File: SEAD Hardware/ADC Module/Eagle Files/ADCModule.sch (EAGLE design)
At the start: 51 parts, among them U1 ADS8568_PM_64, U2 LP2950-3.3ACZ

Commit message: Started SPI/USB Bridge
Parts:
- added C18: 10nF, SensorCape:CAP0805
- added C19, C20: 47pF, SensorCape:CAP0805
- added C21, C23, C24: 100nF, SensorCape:CAP0805
- added C22: 4.7uF, SensorCape:CAP_POLPTH2
- added L1: Ferrite Bead 0805, ASL:INDUCTOR0805
- added R4, R5: 27 1%, SensorCape:RESISTOR0805-RES
- added U$2: FT121Q, SensorCape:FT121Q
- added U3: SI8663BC-B-IS1, SensorCape:SI8663BC-B-IS1
- added X1: MINI-USB-SCHIELD-32005-201, con-cypressindustries:MINI-USB-SCHIELD-32005-201
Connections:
- new net GND_USB: C18.2, C19.1, C20.2, C21.1, C22.-, C23.1, U$2.GND, U$2.GND1, U3.GND1, X1G$1.5, X1S.S1, X1S.S2, X1S.S3, X1S.S4
- new net N$10: R4.2, U$2.DM
- new net N$11: U$2.SS_N
- new net N$12: R5.2, U$2.DP
- new net N$13: U$2.MISO, U3.A3
- new net N$17: U$2.MOSI, U3.A6
- new net N$18: U$2.SCLK, U3.A4
- new net N$19: U3.A5
- new net N$6: C18.1, L1.1, X1G$1.1
- new net N$8: C19.2, R4.1, X1G$1.2
- new net N$9: C20.1, R5.1, X1G$1.3
- new net SCLK: U3.B4
- new net VCC3V3_USB: C21.2, C24.1, C24.2, U$2.RESET_N, U$2.VBUS_S, U$2.VCCIO, U$2.VOUT3V3, U3.VDD1
- new net VCC_USB: C22.+, C23.2, L1.2, U$2.VCC
- net MISO: now also U3.B3
- net MOSI: now also U3.B6

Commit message: Finished DAQ Hardware v1.4 and Filtering Simulations
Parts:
- removed C72, C73, C74: 10nF, SensorCape:CAP0805
- removed JP4: (no value), ASL:M06SIP
- removed JP5: M03PTH, ASL:M03PTH
- removed L1: Ferrite Bead 0805, ASL:INDUCTOR0805
- removed R4, R5: 27 1%, SensorCape:RESISTOR0805-RES
- removed U3: SI8663BC-B-IS1, SensorCape:SI8663BC-B-IS1
- removed X1: MINI-USB-SCHIELD-32005-201, con-cypressindustries:MINI-USB-SCHIELD-32005-201
- added C25, C26, C27, C29, C32: 10uF, ASL:CAP0805
- added C30: 1uF, SensorCape:CAP0805
- added C31: 10nF, SensorCape:CAP0805
- added C34: 10uF, SensorCape:CAP1206
- added JP2: M03-SCREW-5MM, ASL:M03-SCREW-5MM
- added R23: 1.5M, ASL:RESISTOR0805-RES
- added R24: 162k, ASL:RESISTOR0805-RES
- added U6: TPS7A3301_RGW_20, SensorCape:TPS7A3301_RGW_20
- C18: value 10nF -> 1uF
- C19: value 47pF -> 10uF; device SensorCape:CAP0805 -> SensorCape:CAP1206
- C20: value 47pF -> 10uF; device SensorCape:CAP0805 -> ASL:CAP0805
- C21, C23, C24: value 100nF -> 10uF; device SensorCape:CAP0805 -> ASL:CAP0805
- C22: value 4.7uF -> 10uF; device SensorCape:CAP_POLPTH2 -> ASL:CAP0805
- U$2: value FT121Q -> TPS7A4700_RGW_20; device SensorCape:FT121Q -> SensorCape:TPS7A4700_RGW_20
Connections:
- removed net AA1_R_OUT: C73.2, JP4.1, U1.CH_A0
- removed net AA2_R_OUT: C74.2, JP4.3, U1.CH_A1
- removed net AA3_R_OUT: C72.2, JP4.5, U1.CH_B0
- removed net GND_USB: C18.2, C19.1, C20.2, C21.1, C22.-, C23.1, U$2.GND, U$2.GND1, U3.GND1, X1G$1.5, X1S.S1, X1S.S2, X1S.S3, X1S.S4
- removed net N$1: JP1.3, JP4.2
- removed net N$10: R4.2, U$2.DM
- removed net N$11: U$2.SS_N
- removed net N$12: R5.2, U$2.DP
- removed net N$13: U$2.MISO, U3.A3
- removed net N$17: U$2.MOSI, U3.A6
- removed net N$18: U$2.SCLK, U3.A4
- removed net N$19: U3.A5
- removed net N$2: JP1.2, JP4.4
- removed net N$3: JP1.1, JP4.6
- removed net N$9: C20.1, R5.1, X1G$1.3
- removed net SCLK: U3.B4
- removed net VCC3V3_USB: C21.2, C24.1, C24.2, U$2.RESET_N, U$2.VBUS_S, U$2.VCCIO, U$2.VOUT3V3, U3.VDD1
- removed net VCC_USB: C22.+, C23.2, L1.2, U$2.VCC
- new net A0: JP1.3, U1.CH_A0
- new net A1: JP1.2, U1.CH_A1
- new net B0: JP1.1, U1.CH_B0
- new net B1: JP2.3, U1.CH_B1
- new net C0: JP2.2, U1.CH_C0
- new net C1: JP2.1, U1.CH_C1
- new net D0: U1.CH_D0
- new net D1: U1.CH_D1
- new net HVDD_15D: C19.1, U$2.EN, U$2.IN, U$2.IN_2
- new net HVSS_15D: C34.2, U6.EN, U6.IN, U6.IN_2
- new net N$33: C30.1, U6.NR/SS
- net GND: now also C18.2, C19.2, C20.2, C21.2, C22.2, C23.2, C24.2, C25.2, C26.2, C27.2, C29.2, C30.2, C32.2, C34.1, R24.1, U$2.0P2V, U$2.0P8V, U$2.3P2V, U$2.6P4V2, U$2.EPAD, U$2.GND, U6.EPAD, U6.GND; no longer C72.1, C73.1, C74.1, JP5.3, U1.CH_B1, U1.CH_C0, U1.CH_C1, U1.CH_D0, U1.CH_D1
- net HVDD_12A: now also C20.1, C21.1, C22.1, C23.1, C24.1, U$2.OUT, U$2.OUT_1, U$2.SENSE/FB; no longer JP5.2
- net HVSS_12A: now also C25.1, C26.1, C27.1, C29.1, C31.1, C32.1, R23.2, U6.OUT, U6.OUT_2; no longer JP5.1
- net MISO: no longer U3.B3
- net MOSI: no longer U3.B6
- net N$6: now also U$2.NR; no longer L1.1, X1G$1.1
- net N$8: now also C31.2, R23.1, R24.2, U6.FB; no longer C19.2, R4.1, X1G$1.2
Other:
- moved on the sheet: C18, C19, C20, C21, C23, C24

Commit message: More compute unit work.
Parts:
- removed C1, C2, C3, C4, C46, C47, C48, C5, C53, C54, C56, C6, C7: 10uF, SensorCape:CAP0805
- removed C18, C28, C30, C58: 1uF, SensorCape:CAP0805
- removed C19, C34: 10uF, SensorCape:CAP1206
- removed C20, C21, C22, C23, C24, C25, C26, C27, C29, C32: 10uF, ASL:CAP0805
- removed C31: 10nF, SensorCape:CAP0805
- removed C33: 10uF, SensorCape:CAP_POLPTH2
- removed C55, C57, C59, C60, C61, C62, C64, C71: .1uF, SensorCape:CAP0805
- removed C63: .47uF, SensorCape:CAP0805
- removed JP1, JP2: M03-SCREW-5MM, ASL:M03-SCREW-5MM
- removed R23: 1.5M, ASL:RESISTOR0805-RES
- removed R24: 162k, ASL:RESISTOR0805-RES
- removed SL1: (no value), ASL:M04LOCK
- removed U$2, U$3: TPS7A4700_RGW_20, SensorCape:TPS7A4700_RGW_20
- removed U1: ADS8568_PM_64, SensorCape:ADS8568_PM_64
- removed U2: LP2950-3.3ACZ, ASL:LP2950-3.3ACZ
- removed U6: TPS7A3301_RGW_20, SensorCape:TPS7A3301_RGW_20
- added X1: 52885-0374, SensorCape:52885-0374
- C8: device SensorCape:CAP1206 -> SensorCape:CAP0805
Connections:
- removed net A0: JP1.3, U1.CH_A0
- removed net A1: JP1.2, U1.CH_A1
- removed net B0: JP1.1, U1.CH_B0
- removed net B1: JP2.3, U1.CH_B1
- removed net BUSY: U$1.AETXD0/*SS1A/U1BRX/*U1ACTS/CN20/RD14, U1.BUSY/INT
- removed net C0: JP2.2, U1.CH_C0
- removed net C1: JP2.1, U1.CH_C1
- removed net CONV_A: U$1.AN15/ERXD3/AETXD2/OCFB/PMALL/PMA0/CN12/RB15, U1.CONVST_A
- removed net CONV_B: U$1.AN14/ERXD2/AETXD3/PMALH/PMA1/RB14, U1.CONVST_B
- removed net CONV_C: U1.CONVST_C
- removed net CONV_D: U1.CONVST_D
- removed net CS*: U$1.AC1RX/*SS3A/U3BRX/*U3ACTS/RF12, U1.*CS/*FS
- removed net D0: U1.CH_D0
- removed net D1: U1.CH_D1
- removed net HVDD_12A: C20.1, C21.1, C22.1, C23.1, C24.1, C56.2, C57.2, C6.1, C7.1, U$2.OUT, U$2.OUT_1, U$2.SENSE/FB, U$3.EN, U$3.IN, U$3.IN_2, U1.HVDD, U2.IN
- removed net HVDD_15D: C19.1, U$2.EN, U$2.IN, U$2.IN_2
- removed net HVSS_12A: C25.1, C26.1, C27.1, C29.1, C31.1, C32.1, C54.2, C55.2, R23.2, U1.HVSS, U6.OUT, U6.OUT_2
- removed net HVSS_15D: C34.2, U6.EN, U6.IN, U6.IN_2
- removed net N$33: C30.1, U6.NR/SS
- removed net N$45: C28.1, U$3.NR
- removed net N$6: C18.1, U$2.NR
- removed net N$7: C63.1, U1.REFIO
- removed net N$8: C31.2, R23.1, R24.2, U6.FB
- removed net N$87: C46.2, U1.REFDP
- removed net N$93: C53.2, U1.REFAP
- removed net N$94: C48.2, U1.REFBP
- removed net N$96: C47.1, U1.REFCP
- removed net PMP1: U$1.PMRD/CN14/RD5, U1.DB1/DCIN_C
- removed net PMP10: U$1.TRD2/RG14, U1.DB10/SCLK
- removed net PMP11: U$1.TRD1/RG12, U1.DB11/*REFBUFEN
- removed net PMP12: U$1.TRD0/RG13, U1.DB12/SDO_A
- removed net PMP13: U$1.PMD2/RE2, U1.DB13/SDO_B
- removed net PMP14: U$1.PMD3/RE3, U1.DB14/SDO_C
- removed net PMP15: U$1.PMD4/RE4, U1.DB15/SDO_D
- removed net PMP2: U$1.C1RX/ETXD1/PMD11/RF0, U1.DB2/DCIN_B
- removed net PMP3: U$1.C1TX/ETXD0/PMD10/RF1, U1.DB3/DCIN_A
- removed net PMP4: U$1.C2TX/ETXERR/PMD9/RG1, U1.DB4
- removed net PMP5: U$1.C2RX/PMD8/RG0, U1.DB5/SEL_CD
- removed net PMP6: U$1.TRCLK/RA6, U1.DB6/SEL_B
- removed net PMP7: U$1.TRD3/RA7, U1.DB7
- removed net PMP8: U$1.PMD0/RE0, U1.DB8/DCEN
- removed net PMP9: U$1.PMD1/RE1, U1.DB9/SDI
- removed net RD*: U$1.AN12/ERXD0/AECRS/PMA11/RB12, U1.*RD
- removed net RX1A: U$1.SDA1A/SDI1A/U1ARX/RF2
- removed net TX1A: U$1.SCL1A/SDO1A/U1ATX/RF8
- removed net VDD5V0_A: C1.1, C2.1, C3.1, C4.1, C5.1, C59.1, C60.1, C61.2, C62.2, C64.1, C71.1, U$3.OUT, U$3.OUT_1, U$3.SENSE/FB, U1.AVDD, U1.AVDD_2, U1.AVDD_3, U1.AVDD_4, U1.AVDD_5, U1.AVDD_6
- removed net WR*: U$1.AN13/ERXD1/AECOL/PMA10/RB13, U1.REFEN/*WR
- new net CANRX: U$1.C1RX/ETXD1/PMD11/RF0
- new net CANTX: U$1.C1TX/ETXD0/PMD10/RF1
- new net N$1: U$1.OSC1/CLKI/RC12
- new net N$2: U$1.OSC2/CLKO/RC15
- new net SCL: U$1.SCL2/RA2, X1-16.S
- new net SDA: U$1.SDA2/RA3, X1-14.S
- new net U1RX: U$1.SDA1A/SDI1A/U1ARX/RF2, X1-22.S
- new net U1TX: U$1.SCL1A/SDO1A/U1ATX/RF8, X1-20.S
- new net U3RX: U$1.SDA3A/SDI3A/U3ARX/PMA9/CN17/RF4, X1-28.S
- new net U3TX: U$1.SCL3A/SDO3A/U3ATX/PMA8/CN18/RF5, X1-26.S
- net GND: now also X1-1.S, X1-12.S, X1-18.S, X1-2.S, X1-24.S, X1-29.S, X1-30.S; no longer C1.2, C18.2, C19.2, C2.2, C20.2, C21.2, C22.2, C23.2, C24.2, C25.2, C26.2, C27.2, C28.2, C29.2, C3.2, C30.2, C32.2, C33.-, C34.1, C4.2, C46.1, C47.2, C48.1, C5.2, C53.1, C54.1, C55.1, C56.1, C57.1, C58.1, C59.2, C6.2, C60.2, C61.1, C62.1, C63.2, C64.2, C7.2, C71.2, R24.1, U$2.0P2V, U$2.0P8V, U$2.3P2V, U$2.6P4V2, U$2.EPAD, U$2.GND, U$3.0P4V, U$3.3P2V, U$3.EPAD, U$3.GND, U1.*PAR/SER, U1.AGND, U1.AGND_2, U1.AGND_3, U1.AGND_4, U1.AGND_5, U1.AGND_6, U1.ASLEEP, U1.DGND, U1.RANGE/XCLK, U1.REFAN, U1.REFBN, U1.REFCN, U1.REFDN, U1.REFN, U1.RESET, U2.GND, U6.EPAD, U6.GND
- net MISO: now also X1-4.S; no longer SL1.2
- net MOSI: now also X1-6.S; no longer SL1.3
- net PMP0: no longer U1.DB0/DCIN_D
- net SCK: now also X1-10.S; no longer SL1.1
- net SS: now also X1-8.S; no longer SL1.4
- net VDD3V3_D: no longer C33.+, C58.2, U1.*HW/SW, U1.*STBY, U1.DVDD, U2.OUT

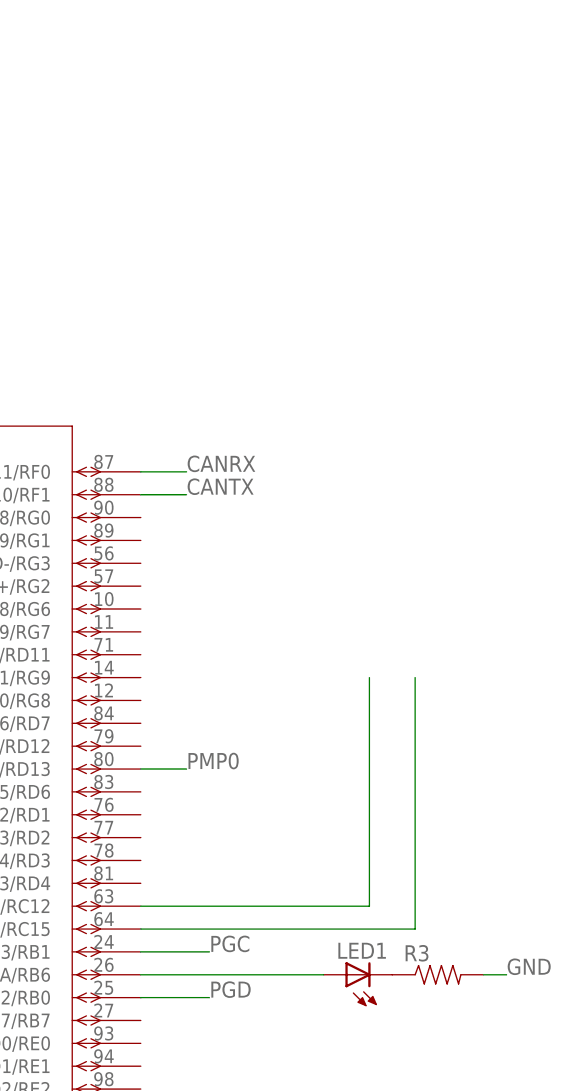
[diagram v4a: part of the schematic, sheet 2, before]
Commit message: Compute module clock sources.
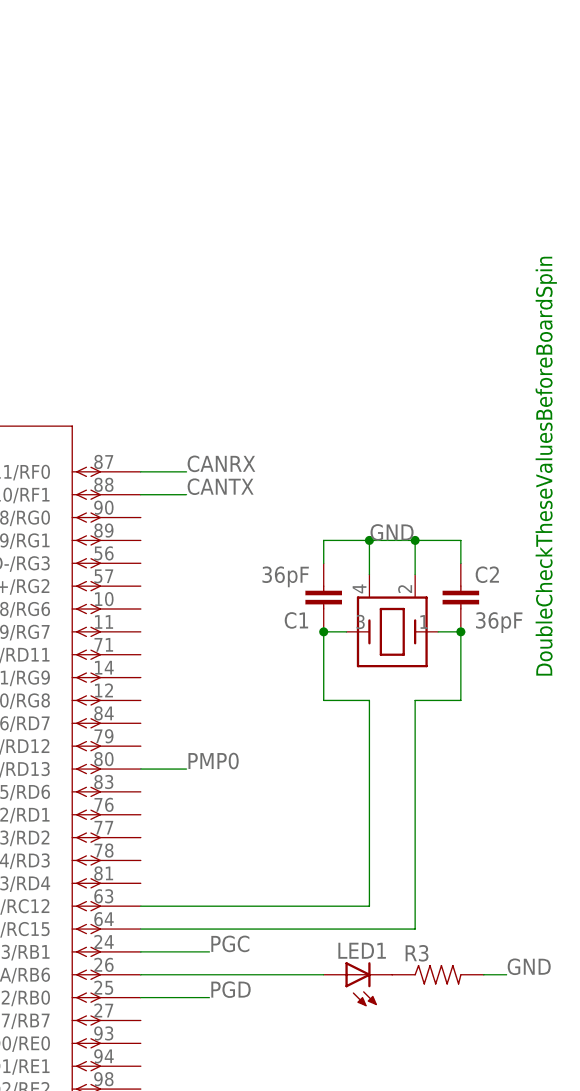
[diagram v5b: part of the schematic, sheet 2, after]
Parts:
- added C1, C2: 36pF, SensorCape:CAP0805
- added C3, C4: 20pF, SensorCape:CAP0805
- added IC1: (no value), SensorCape:IC_FT2232H
- added IC2: 93-C46AST, microchip:93-C46AST
- added U$2: ABM3B-8.000MHZ-10-1-U-T, SensorCape:ABM3B-8.000MHZ-10-1-U-T
- added U$3: 7M-12.000MEEQ-T, SensorCape:7M-12.000MEEQ-T
- added USB1: CON-USB-F-MICRO-B, dp_devices.v6:CON-USB-F-MICRO-B
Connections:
- new net N$10: IC1.DM, USB1USB.D-
- new net N$11: IC1.DP, USB1USB.D+
- new net N$8: C3.1, U$3.OSC2
- new net N$9: C4.2, U$3.OSC1
- net GND: now also C1.2, C2.1, C3.2, C4.1, U$2.GND1, U$2.GND2, U$3.GND1, U$3.GND2
- net N$1: now also C1.1, U$2.OSC2
- net N$2: now also C2.2, U$2.OSC1
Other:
- note added: "DoubleCheckTheseValuesBeforeBoardSpin"
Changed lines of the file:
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@@
 <part name="FRAME2" library="SensorCape" deviceset="FRAME_B_L" device=""/>
 <part name="X1" library="SensorCape" deviceset="52885-0374" device=""/>
+<part name="IC1" library="SensorCape" deviceset="IC_FT2232H" device=""/>
+<part name="C1" library="SensorCape" deviceset="CAP" device="0805" value="36pF"/>
+<part name="C2" library="SensorCape" deviceset="CAP" device="0805" value="36pF"/>
+<part name="U$2" library="SensorCape" deviceset="ABM3B-8.000MHZ-10-1-U-T" device=""/>
+<part name="C3" library="SensorCape" deviceset="CAP" device="0805" value="20pF"/>
+<part name="C4" library="SensorCape" deviceset="CAP" device="0805" value="20pF"/>
+<part name="U$3" library="SensorCape" deviceset="7M-12.000MEEQ-T" device=""/>
+<part name="IC2" library="microchip" deviceset="93-*" device="ST" technology="C46A"/>
+<part name="USB1" library="dp_devices.v6" deviceset="CON-USB-F" device="-MICRO-B"/>
 </parts>
 <sheets>
 <sheet>
 <plain>
+<text x="25.4" y="81.28" size="1.778" layer="91" rot="R90">DoubleCheckTheseValuesBeforeBoardSpin</text>
 </plain>
 <instances>
 <instance part="FRAME1" gate="G$1" x="0" y="0"/>
 <instance part="FRAME1" gate="G$2" x="325.12" y="0"/>
+<instance part="IC1" gate="G$1" x="119.38" y="160.02"/>
+<instance part="C3" gate="G$1" x="35.56" y="93.98" rot="R180"/>
+<instance part="C4" gate="G$1" x="50.8" y="91.44"/>
+<instance part="U$3" gate="G$1" x="43.18" y="88.9" rot="R180"/>
+<instance part="IC2" gate="G$1" x="78.74" y="81.28"/>
+<instance part="USB1" gate="USB" x="53.34" y="190.5"/>
 </instances>
 <busses>
 </busses>
 <nets>
+<net name="GND" class="0">
+<segment>
+<pinref part="C3" gate="G$1" pin="2"/>
+<wire x1="35.56" y1="96.52" x2="35.56" y2="99.06" width="0.1524" layer="91"/>
+<wire x1="35.56" y1="99.06" x2="40.64" y2="99.06" width="0.1524" layer="91"/>
+<pinref part="C4" gate="G$1" pin="1"/>
+<wire x1="40.64" y1="99.06" x2="45.72" y2="99.06" width="0.1524" layer="91"/>
+<wire x1="45.72" y1="99.06" x2="50.8" y2="99.06" width="0.1524" layer="91"/>
+<wire x1="50.8" y1="99.06" x2="50.8" y2="96.52" width="0.1524" layer="91"/>
+<wire x1="45.72" y1="99.06" x2="45.72" y2="95.25" width="0.1524" layer="91"/>
+<wire x1="40.64" y1="99.06" x2="40.64" y2="95.25" width="0.1524" layer="91"/>
+<junction x="40.64" y="99.06"/>
+<junction x="45.72" y="99.06"/>
+<label x="40.64" y="99.06" size="1.778" layer="95"/>
+<pinref part="U$3" gate="G$1" pin="GND1"/>
+<pinref part="U$3" gate="G$1" pin="GND2"/>
+</segment>
+</net>
+<net name="N$8" class="0">
+<segment>
+<wire x1="40.64" y1="58.42" x2="40.64" y2="81.28" width="0.1524" layer="91"/>
+<wire x1="38.1" y1="88.9" x2="35.56" y2="88.9" width="0.1524" layer="91"/>
+<wire x1="35.56" y1="88.9" x2="35.56" y2="81.28" width="0.1524" layer="91"/>
+<wire x1="35.56" y1="81.28" x2="40.64" y2="81.28" width="0.1524" layer="91"/>
+<pinref part="C3" gate="G$1" pin="1"/>
+<junction x="35.56" y="88.9"/>
+<pinref part="U$3" gate="G$1" pin="OSC2"/>
+</segment>
+</net>
+<net name="N$9" class="0">
+<segment>
+<wire x1="45.72" y1="55.88" x2="45.72" y2="81.28" width="0.1524" layer="91"/>
+<wire x1="48.26" y1="88.9" x2="50.8" y2="88.9" width="0.1524" layer="91"/>
+<wire x1="50.8" y1="88.9" x2="50.8" y2="81.28" width="0.1524" layer="91"/>
+<wire x1="50.8" y1="81.28" x2="45.72" y2="81.28" width="0.1524" layer="91"/>
+<pinref part="C4" gate="G$1" pin="2"/>
+<junction x="50.8" y="88.9"/>
+<pinref part="U$3" gate="G$1" pin="OSC1"/>
+</segment>
+</net>
+<net name="N$10" class="0">
+<segment>
+<pinref part="IC1" gate="G$1" pin="DM"/>
+<pinref part="USB1" gate="USB" pin="D-"/>
+<wire x1="83.82" y1="190.5" x2="58.42" y2="190.5" width="0.1524" layer="91"/>
+</segment>
+</net>
+<net name="N$11" class="0">
+<segment>
+<pinref part="USB1" gate="USB" pin="D+"/>
+<pinref part="IC1" gate="G$1" pin="DP"/>
+<wire x1="58.42" y1="187.96" x2="83.82" y2="187.96" width="0.1524" layer="91"/>
+</segment>
+</net>
 </nets>
 </sheet>
 <sheet>
 <plain>
+<text x="381" y="157.48" size="1.778" layer="91" rot="R90">DoubleCheckTheseValuesBeforeBoardSpin</text>
 </plain>
 <instances>
@@
 <instance part="X1" gate="-29" x="208.28" y="218.44"/>
 <instance part="X1" gate="-30" x="233.68" y="218.44"/>
+<instance part="C1" gate="G$1" x="355.6" y="167.64" rot="R180"/>
+<instance part="C2" gate="G$1" x="370.84" y="165.1"/>
+<instance part="U$2" gate="G$1" x="363.22" y="162.56" rot="R180"/>
 </instances>
 <busses>
@@
 <label x="226.06" y="241.3" size="1.778" layer="95"/>
 </segment>
+<segment>
+<pinref part="C1" gate="G$1" pin="2"/>
+<wire x1="355.6" y1="170.18" x2="355.6" y2="172.72" width="0.1524" layer="91"/>
+<wire x1="355.6" y1="172.72" x2="360.68" y2="172.72" width="0.1524" layer="91"/>
+<pinref part="C2" gate="G$1" pin="1"/>
+<wire x1="360.68" y1="172.72" x2="365.76" y2="172.72" width="0.1524" layer="91"/>
+<wire x1="365.76" y1="172.72" x2="370.84" y2="172.72" width="0.1524" layer="91"/>
+<wire x1="370.84" y1="172.72" x2="370.84" y2="170.18" width="0.1524" layer="91"/>
+<wire x1="365.76" y1="172.72" x2="365.76" y2="168.91" width="0.1524" layer="91"/>
+<wire x1="360.68" y1="172.72" x2="360.68" y2="168.91" width="0.1524" layer="91"/>
+<junction x="360.68" y="172.72"/>
+<junction x="365.76" y="172.72"/>
+<label x="360.68" y="172.72" size="1.778" layer="95"/>
+<pinref part="U$2" gate="G$1" pin="GND1"/>
+<pinref part="U$2" gate="G$1" pin="GND2"/>
+</segment>
 </net>
 <net name="VDD3V3_D" class="0">
@@
 <pinref part="U$1" gate="A" pin="OSC1/CLKI/RC12"/>
 <wire x1="335.28" y1="132.08" x2="360.68" y2="132.08" width="0.1524" layer="91"/>
-<wire x1="360.68" y1="132.08" x2="360.68" y2="157.48" width="0.1524" layer="91"/>
+<wire x1="360.68" y1="132.08" x2="360.68" y2="154.94" width="0.1524" layer="91"/>
+<wire x1="358.14" y1="162.56" x2="355.6" y2="162.56" width="0.1524" layer="91"/>
+<wire x1="355.6" y1="162.56" x2="355.6" y2="154.94" width="0.1524" layer="91"/>
+<wire x1="355.6" y1="154.94" x2="360.68" y2="154.94" width="0.1524" layer="91"/>
+<pinref part="C1" gate="G$1" pin="1"/>
+<junction x="355.6" y="162.56"/>
+<pinref part="U$2" gate="G$1" pin="OSC2"/>
 </segment>
 </net>
@@
 <pinref part="U$1" gate="A" pin="OSC2/CLKO/RC15"/>
 <wire x1="335.28" y1="129.54" x2="365.76" y2="129.54" width="0.1524" layer="91"/>
-<wire x1="365.76" y1="129.54" x2="365.76" y2="157.48" width="0.1524" layer="91"/>
-</segment>
-</net>
+<wire x1="365.76" y1="129.54" x2="365.76" y2="154.94" width="0.1524" layer="91"/>
+<wire x1="368.3" y1="162.56" x2="370.84" y2="162.56" width="0.1524" layer="91"/>
+<wire x1="370.84" y1="162.56" x2="370.84" y2="154.94" width="0.1524" layer="91"/>
+<wire x1="370.84" y1="154.94" x2="365.76" y2="154.94" width="0.1524" layer="91"/>
+<pinref part="C2" gate="G$1" pin="2"/>
+<junction x="370.84" y="162.56"/>
+<pinref part="U$2" gate="G$1" pin="OSC1"/>
+</segment>
+</net>

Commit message: Layout work.
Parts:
- added C18: 2.2uF, SensorCape:CAP0805
- added C19: 4.7uF, SensorCape:CAP0805
- added C20: 3.3uF, SensorCape:CAP_POL1206
- added C21, C22: 4.7uF, SensorCape:CAP_POL1206
- added C23, C24, C5: .1uF, SensorCape:CAP0805
- added C6: 100uF, SensorCape:CAP1206
- added C7: .01uF, SensorCape:CAP0805
- added L1, L2: (no value), dp_devices.v6:FERRITE-0805
- added LED2, LED3: (no value), led:LEDCHIP-LED0805
- added R10, R11: 470, SensorCape:RESISTOR0805-RES
- added R4, R5, R6, R8: 10k, SensorCape:RESISTOR0805-RES
- added R7: 2.2k, SensorCape:RESISTOR0805-RES
- added R9: 12k 1%, SensorCape:RESISTOR0805-RES
- added U1: LP2989_DGK_8, SensorCape:LP2989_DGK_8
- C1, C2: value 36pF -> 20pF
- R3: value (none) -> 330
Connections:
- removed net PMP0: U$1.ETXD3/PMD13/CN19/RD13
- new net A0: IC1.ACBUS1/GPIOH1, U$1.AN15/ERXD3/AETXD2/OCFB/PMALL/PMA0/CN12/RB15
- new net CS*: IC1.ACBUS0/TXDEN/GPIOH0, U$1.EMDC/IC4/PMCS1/PMA14/RD11
- new net D0: IC1.ADBUS0/TXD/TCK/SK, U$1.PMD0/RE0
- new net D1: IC1.ADBUS1/RXD/TDI/DO, U$1.PMD1/RE1
- new net D2: IC1.ADBUS2/RTS#/TDO/DI, U$1.PMD2/RE2
- new net D3: IC1.ADBUS3/CTS#/TMS/CS, U$1.PMD3/RE3
- new net D4: IC1.ADBUS4/DTR#/GPIOL0, U$1.PMD4/RE4
- new net D5: IC1.ADBUS5/DSR#/GPIOL1, U$1.PMD5/RE5
- new net D6: IC1.ADBUS6/DCD#/GPIOL2, U$1.PMD6/RE6
- new net D7: IC1.ADBUS7/RI#/GPIOL3, U$1.PMD7/RE7
- new net N$12: IC1.EECS, IC2.CS, R4.1
- new net N$13: IC1.EECLK, IC2.CLK, R5.1
- new net N$17: IC2.DO, R6.1, R7.1
- new net N$18: IC1.EEDATA, IC2.DI, R7.2
- new net N$19: IC1.RESET#, R8.1
- new net N$20: IC1.REF, R9.1
- new net N$21: C22.+, C24.1, IC1.VPHY, L2.1
- new net N$22: C21.+, C23.1, IC1.VPLL, L1.1
- new net N$23: C7.2, U1.BYPASS
- new net N$24: C18.2, C7.1, U1.GND
- new net N$27: IC1.BCBUS0/GPIOH1
- new net N$28: IC1.BCBUS3/RXLED#/GPIOH3, R10.2
- new net N$29: IC1.BCBUS4/TXLED#/GPIOH4, R11.2
- new net N$32: LED2.C, R10.1
- new net N$33: LED3.C, R11.1
- new net RD*: IC1.ACBUS2/GPIOH2, U$1.PMRD/CN14/RD5
- new net SIWUA: IC1.ACBUS4/TXLED#/GPIOH4
- new net USB_UART_RX: IC1.BDBUS1/RXD/TDI/DO, U$1.ERXDV/SCL2A/SDO2A/U2ATX/PMA3/CN10/RG8
- new net USB_UART_TX: IC1.BDBUS0/TXD/TCK/SK, U$1.ECRS/SDA2A/SDI2A/U2ARX/PMA4/CN9/RG7
- new net VDD1V8_D: C20.+, IC1.VCORE0, IC1.VCORE1, IC1.VCORE2, IC1.VREGOUT
- new net VDD5V0_D: C18.1, C6.2, U1.VIN, U1.~SD, USB1USB.VUSB, X1-3.S
- new net WR*: IC1.ACBUS3/RXLED#/GPIOH3, U$1.OC5/PMWR/CN13/RD4
- net CANRX: now also X1-7.S
- net CANTX: now also X1-9.S
- net GND: now also C19.1, C20.-, C21.-, C22.-, C23.2, C24.2, C5.2, C6.1, IC1.AGND, IC1.GND0, IC1.GND1, IC1.GND2, IC1.GND3, IC1.GND4, IC1.GND5, IC1.GND6, IC1.GND7, IC1.TEST, IC2.GND, R9.2, USB1USB.GND
- net N$8: now also IC1.OSC0
- net N$9: now also IC1.OSCI
- net VDD3V3_D: now also C19.2, C5.1, IC1.VCCIO0, IC1.VCCIO1, IC1.VCCIO2, IC1.VCCIO3, IC1.VREGIN, IC2.VCC, L1.2, L2.2, LED2.A, LED3.A, R4.2, R5.2, R6.2, R8.2, U1.SENSE, U1.VOUT, X1-5.S
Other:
- note removed: "DoubleCheckTheseValuesBeforeBoardSpin"
- moved on the sheet: C1, C2, C3, C4, IC1, IC2
